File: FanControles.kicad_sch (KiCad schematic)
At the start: 5 parts, among them IC1 PJA3432, P1 24v Fan, P2 24v, P3 100k NTC

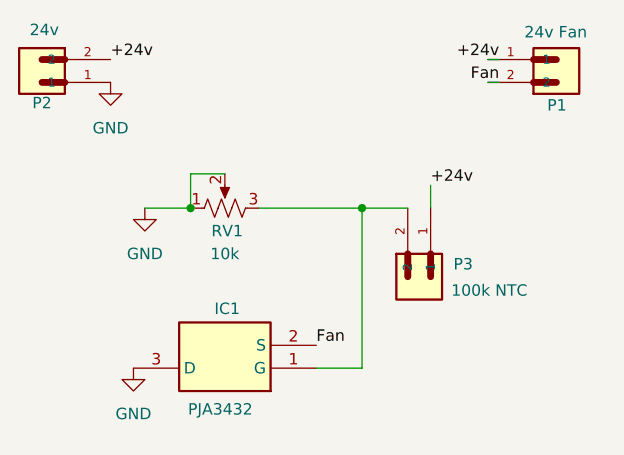
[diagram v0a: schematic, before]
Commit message: almost done
TODO: change the potenciometer to a cheaper one
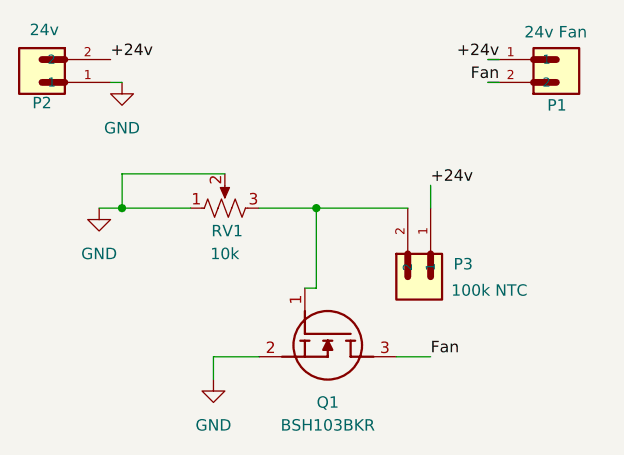
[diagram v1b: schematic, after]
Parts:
- removed IC1: PJA3432, KiCad:SOT95P240X110-3N, symbol PJA3432_R2_00001:PJA3432_R2_00001
- added Q1: BSH103BKR, BSH:SOT95P230X110-3N, symbol BSH103BKR:BSH103BKR
- RV1: Manufacturer_Part_Number (none) -> 3266 W-1-103_LF
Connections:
- net Fan: now also Q1.3 (D)
- net GND: now also Q1.2 (S)
- net at P3.2, RV1.3: now also Q1.1 (G)
